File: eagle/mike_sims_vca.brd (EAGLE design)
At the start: 100 x 80 mm, 33 parts, among them IC2 LM13700N, IC3 TL072P, Q1 2N3906

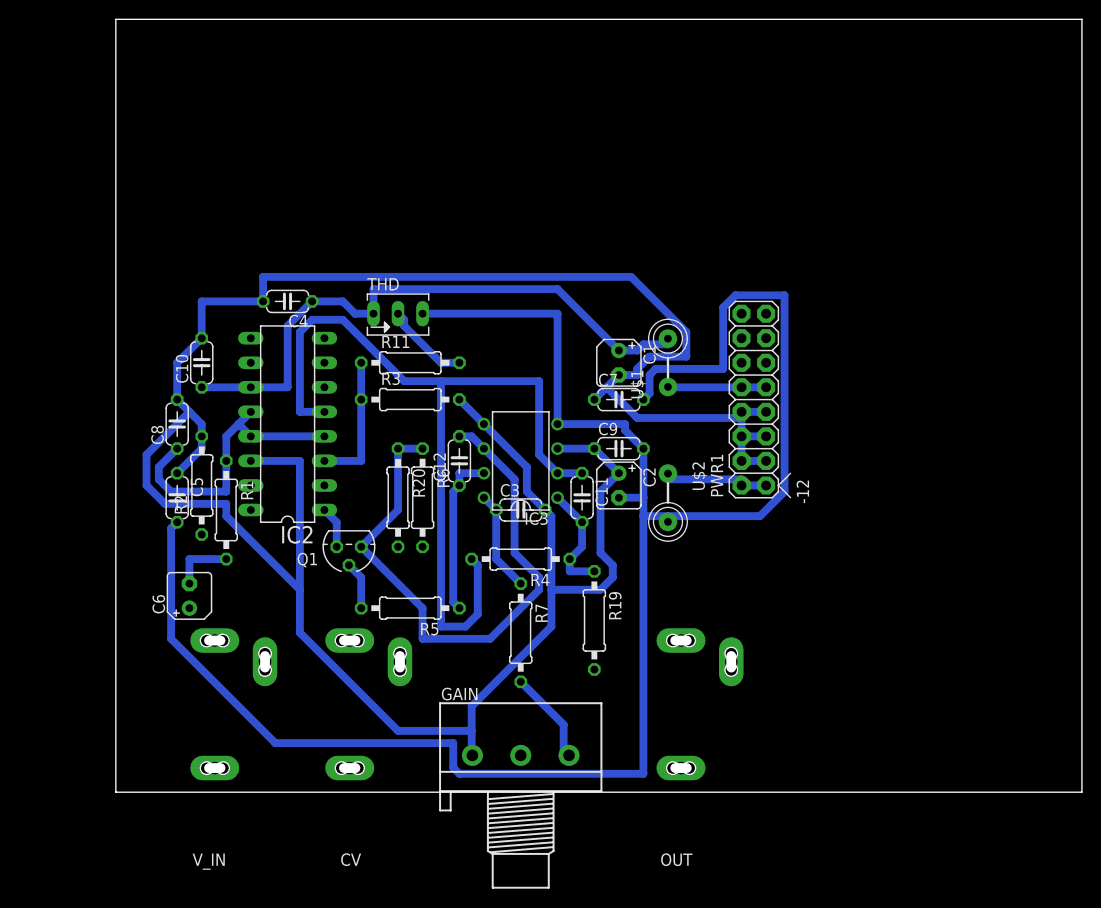
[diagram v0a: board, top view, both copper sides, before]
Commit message: moved to vertical
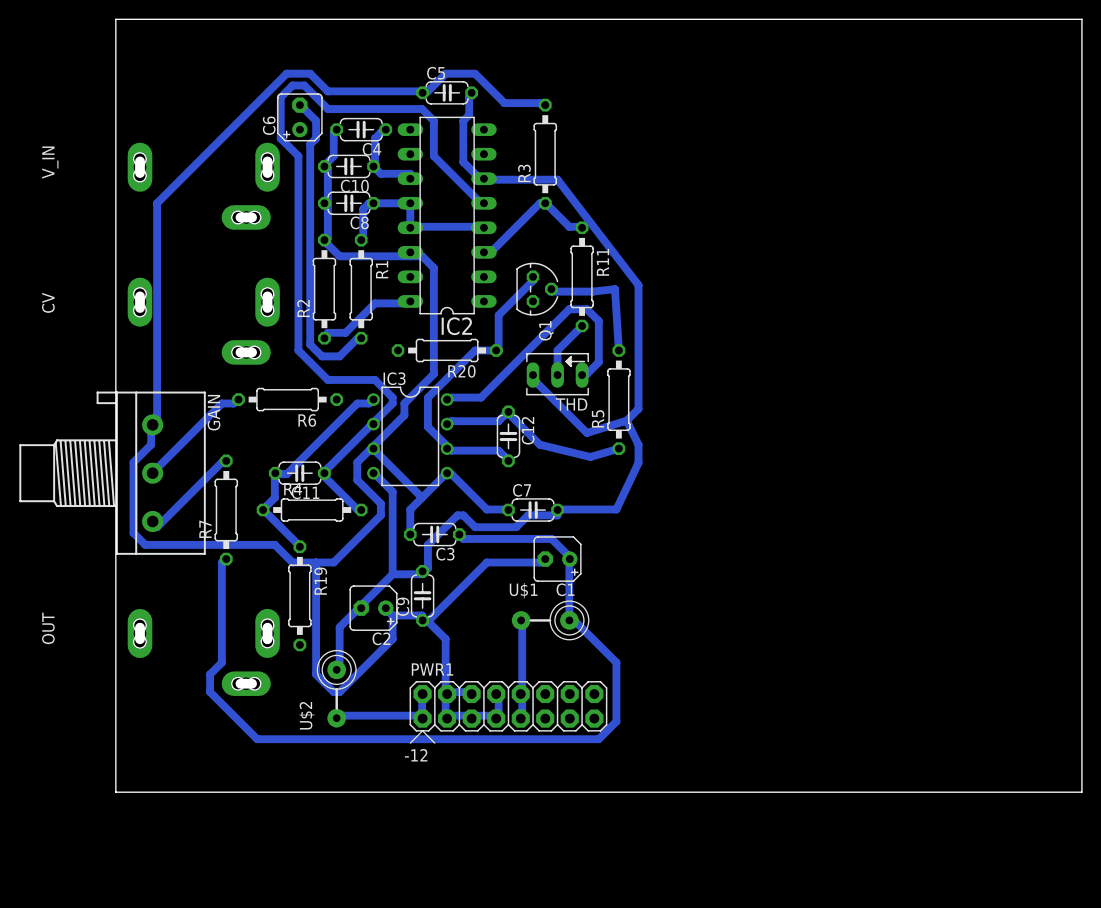
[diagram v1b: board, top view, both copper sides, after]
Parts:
- moved OUT 64.5 mm to (0.00, 11.4), turned to 90 degrees
- moved V_IN 61.6 mm to (0.00, 59.7), turned to 90 degrees
- moved CV 54.3 mm to (0.00, 45.7), turned to 90 degrees
- moved C6 50.8 mm to (19.1, 69.8)
- moved C5 50.4 mm to (34.3, 72.4), turned to 0 degrees
- moved GAIN 48.0 mm to (3.81, 33.0), turned to 270 degrees
- moved PWR1 40.4 mm to (38.1, 8.89), turned to 0 degrees
- moved U$2 39.9 mm to (22.9, 10.2), turned to 90 degrees
- moved R7 33.0 mm to (11.4, 29.2), turned to 90 degrees
- moved Q1 32.8 mm to (43.2, 52.1), turned to 270 degrees
- moved R19 30.6 mm to (19.1, 20.3)
- moved R5 30.5 mm to (52.1, 40.6), turned to 90 degrees
- moved U$1 29.5 mm to (44.5, 17.8), turned to 0 degrees
- moved C11 29.3 mm to (19.1, 33.0), turned to 180 degrees
- moved R3 29.0 mm to (44.5, 66.0), turned to 90 degrees
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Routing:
- net -12V: track 200.9 -> 121.5 mm
- net +12V: track 72.7 -> 126.6 mm
- net N$20: track 60.6 -> 31.4 mm
- net N$4: track 6.35 -> 32.3 mm
- net N$12: track 0.00 -> 12.0 mm
- net N$5: track 30.2 -> 18.6 mm
- net N$8: track 11.7 -> 23.1 mm
- net N$7: track 0.00 -> 10.7 mm
- net N$10: track 4.97 -> 13.2 mm
- net GND: track 264.3 -> 258.1 mm
- net N$21: track 4.34 -> 0.00 mm
- net N$9: track 87.3 -> 84.1 mm
- net N$11: track 17.0 -> 20.0 mm
- net N$19: track 8.83 -> 6.13 mm
- net N$13: track 10.0 -> 10.7 mm
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
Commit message: routed
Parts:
- moved C5 55.0 mm to (27.9, 17.8), turned to 90 degrees
- moved C4 51.4 mm to (33.0, 17.8), turned to 270 degrees
- moved C3 35.3 mm to (24.8, 61.0), turned to 270 degrees
- moved C7 31.9 mm to (40.6, 61.0), turned to 90 degrees
- moved C10 26.8 mm to (26.7, 38.1)
- moved R1 20.4 mm to (24.1, 72.4), turned to 180 degrees
- moved R5 16.2 mm to (36.2, 37.5)
- moved R20 11.4 mm to (22.9, 45.7)
- moved C1 10.9 mm to (36.8, 17.8), turned to 270 degrees
- moved Q1 8.98 mm to (36.8, 45.7), turned to 90 degrees
- moved THD 8.98 mm to (44.5, 34.3), turned to 90 degrees
- moved C12 7.96 mm to (33.7, 33.0)
- moved R6 7.52 mm to (10.8, 37.8), turned to 270 degrees
- moved R11 7.41 mm to (44.5, 47.0)
- moved C9 7.18 mm to (26.7, 25.4), turned to 180 degrees
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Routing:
- net -12V: track 121.5 -> 196.6 mm
- net N$9: track 84.1 -> 114.0 mm
- net N$4: track 32.3 -> 3.07 mm
- net N$20: track 31.4 -> 59.9 mm
- net +12V: track 126.6 -> 149.9 mm, vias 0 -> 2
- net N$5: track 18.6 -> 41.5 mm
- net N$11: track 20.0 -> 8.24 mm
- net N$10: track 13.2 -> 4.24 mm
- net GND: track 258.1 -> 250.9 mm
- net N$25: track 0.00 -> 5.86 mm
- net N$13: track 10.7 -> 5.17 mm
- net N$3: track 0.00 -> 5.45 mm
- net N$8: track 23.1 -> 18.2 mm
- net N$24: track 0.00 -> 4.75 mm
- net N$19: track 6.13 -> 10.8 mm
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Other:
- board size 100 x 80 mm -> 101 x 80 mm
